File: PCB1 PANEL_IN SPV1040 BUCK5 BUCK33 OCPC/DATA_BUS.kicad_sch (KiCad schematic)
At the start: 45 parts, among them Q1 BSS138DWQ-7, Q2 BSS138DWQ-7, Q3 MBT2222ADW1T1, Q4 MBT2222ADW1T1, Q5 BSS138DWQ-7, Q6 BSS138DWQ-7, Q7 MBT2222ADW1T1, Q8 MBT2222ADW1T1, Q9 MMDT2907, U23 Payload

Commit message: .
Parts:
- C53, C54, C55, C56: JLCPCB Part# (none) -> C7248
- Q1, Q2, Q5, Q6: JLCPCB Part# (none) -> C3280240
- Q3, Q4, Q7, Q8: JLCPCB Part# (none) -> C157366
- Q9: JLCPCB Part# (none) -> C526684
- R62, R63, R72, R73: JLCPCB Part# (none) -> C3930971
- R64, R65, R74, R75: JLCPCB Part# (none) -> C101158
- R66, R67, R68, R70, R76, R77, R78, R80: JLCPCB Part# (none) -> C328655
- R69, R71, R79, R81: JLCPCB Part# (none) -> C73804
- R82: JLCPCB Part# (none) -> C15402
- R83: JLCPCB Part# (none) -> C88615
- R84, R85: JLCPCB Part# (none) -> C21190

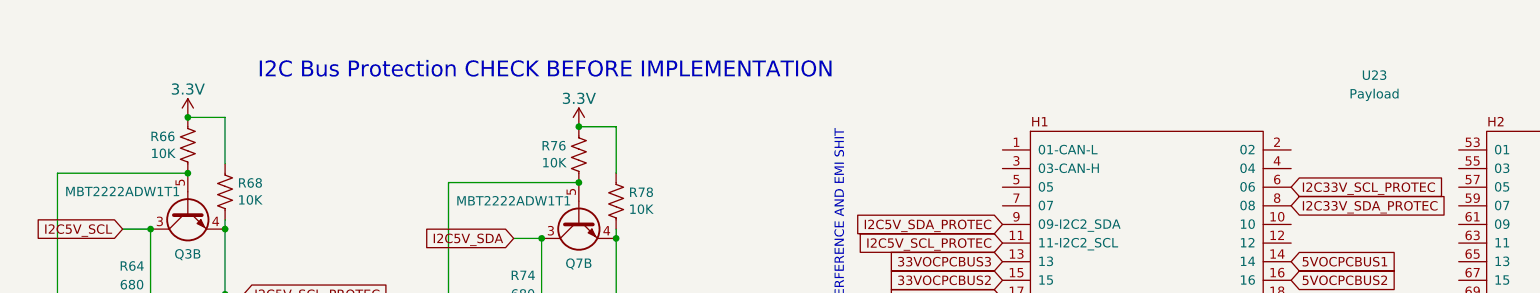
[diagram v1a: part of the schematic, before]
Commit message: Added some comments in POWERPCB, about bus interface
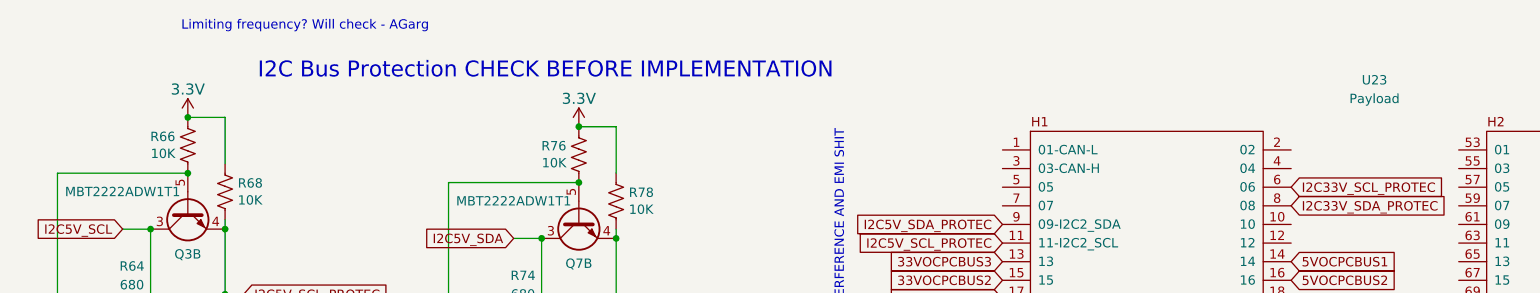
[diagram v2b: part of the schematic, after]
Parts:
- U23: footprint (none) -> Connector_PinHeader_2.54mm:PinHeader_2x26_P2.54mm_Vertical
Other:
- note added: "Limiting frequency? Will check - AGarg"
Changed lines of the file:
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@@
+		)
+	)
+	(text "Limiting frequency? Will check - AGarg"
+		(exclude_from_sim no)
+		(at 56.642 18.034 0)
+		(effects
+			(font
+				(size 1.27 1.27)
+			)
 		)
 	)
@@
 		(fields_autoplaced yes)
 		(property "Reference" "U23"
-			(at 202.5094 24.765 0)
+			(at 202.5094 25.4 0)
 			(effects
 				(font
@@
 		)
 		(property "Value" "Payload"
-			(at 202.5094 27.305 0)
-			(effects
-				(font
-					(size 1.27 1.27)
-				)
-			)
-		)
-		(property "Footprint" ""
+			(at 202.5094 27.94 0)
+			(effects
+				(font
+					(size 1.27 1.27)
+				)
+			)
+		)
+		(property "Footprint" "Connector_PinHeader_2.54mm:PinHeader_2x26_P2.54mm_Vertical"
 			(at 174.625 45.085 0)
 			(effects
